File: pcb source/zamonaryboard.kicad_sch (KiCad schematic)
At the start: 25 parts, among them J1 USB_C_Receptacle_USB2.0_14P, SW1 SW_Push, U1 ESP32-S2, U2 ME6211C33M5, Y1 Crystal_GND24

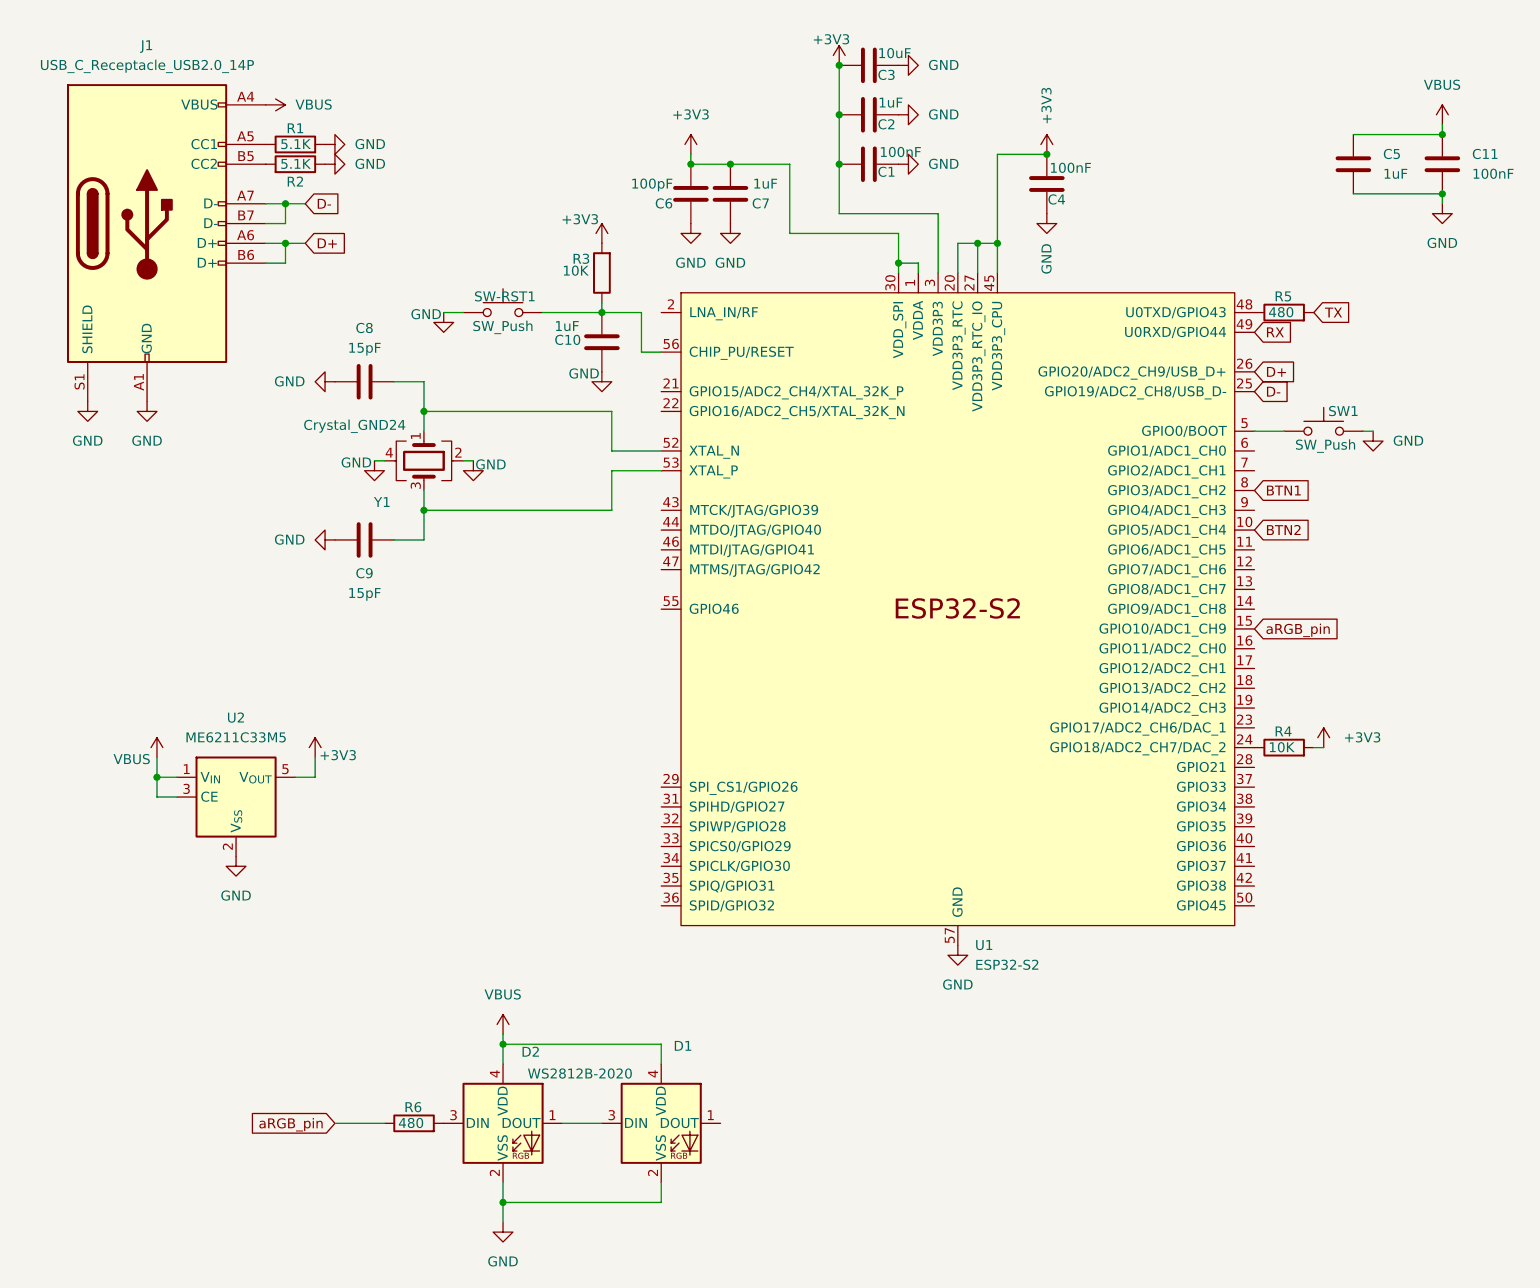
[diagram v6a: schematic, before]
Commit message: Testing of auto-release of firmware
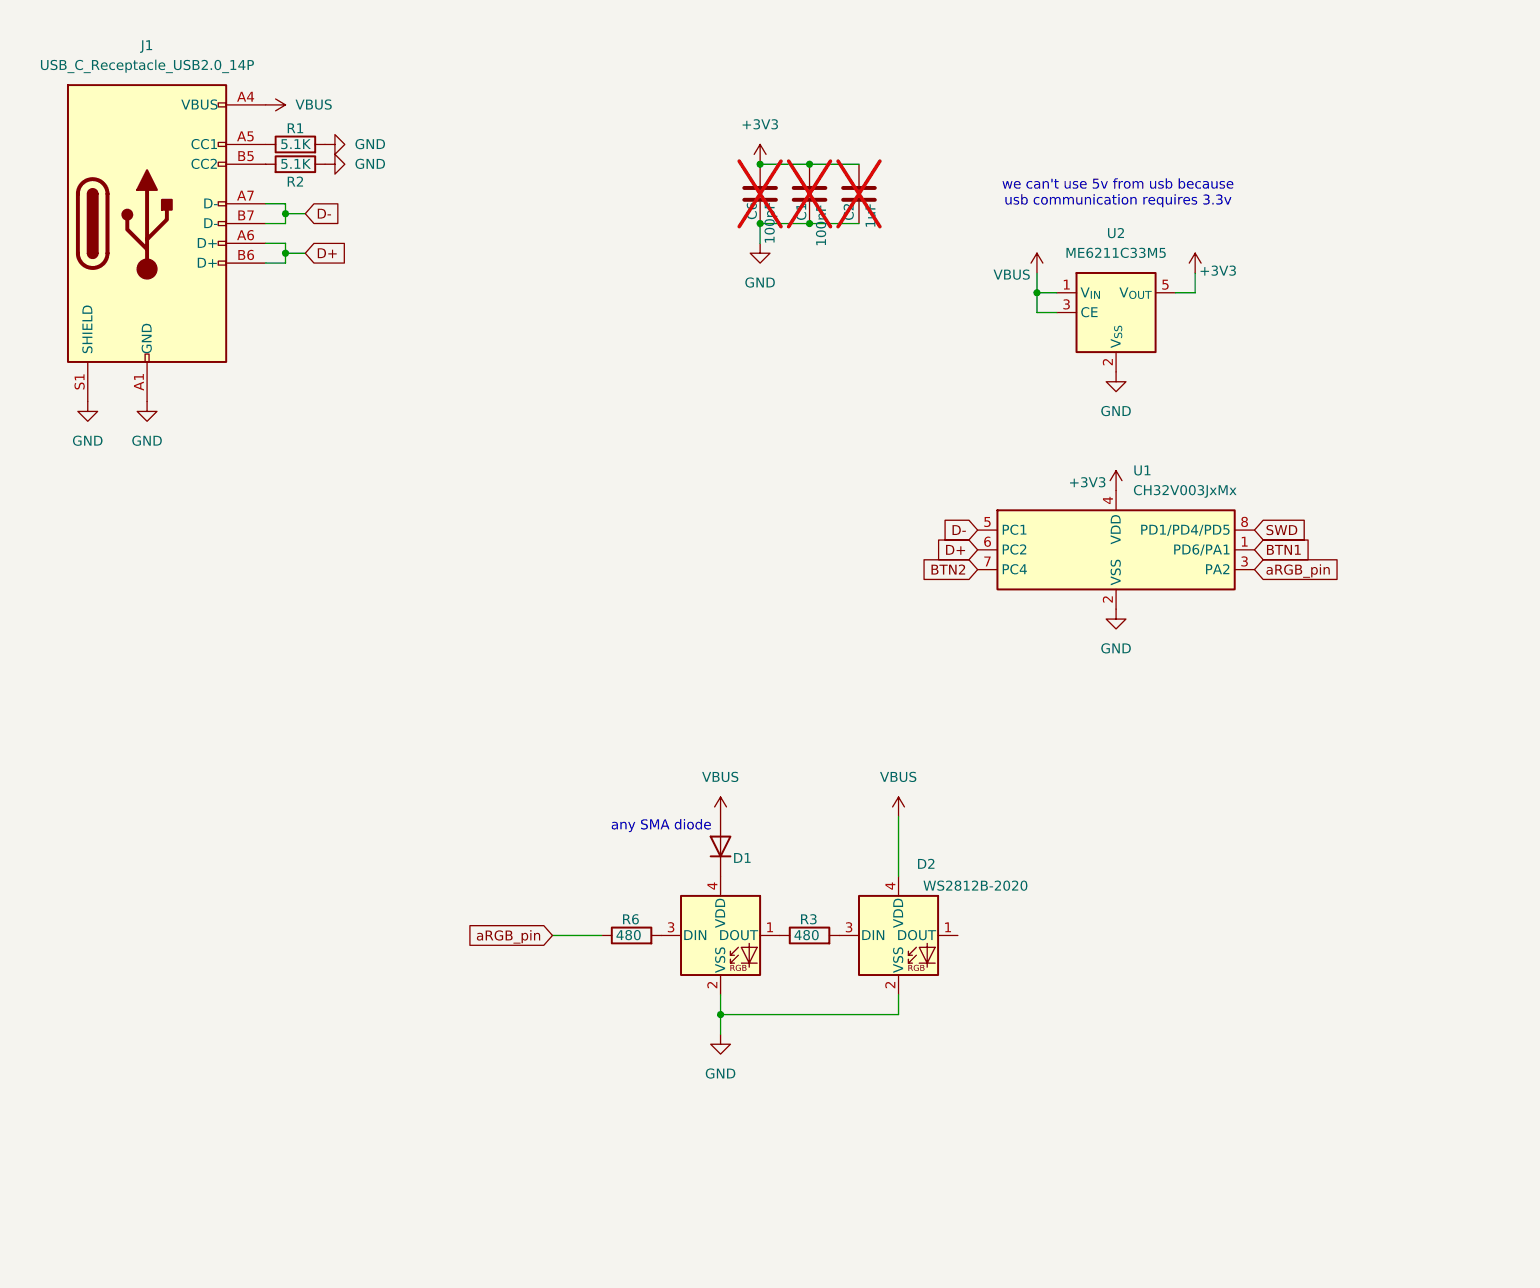
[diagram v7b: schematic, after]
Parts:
- removed C10, C5, C7: 1uF, Capacitor_SMD:C_0603_1608Metric, symbol Device:C
- removed C11, C4: 100nF, Capacitor_SMD:C_0603_1608Metric, symbol Device:C
- removed C3: 10uF, Capacitor_SMD:C_0603_1608Metric, symbol Device:C
- removed C8, C9: 15pF, Capacitor_SMD:C_0603_1608Metric, symbol Device:C
- removed R4: 10K, Resistor_SMD:R_0603_1608Metric, symbol Device:R
- removed R5: 480, Resistor_SMD:R_0603_1608Metric, symbol Device:R
- removed SW-RST1, SW1: SW_Push, Button_Switch_SMD:SW_SPST_SKQG_WithoutStem, symbol Switch:SW_Push
- removed U1: ESP32-S2, Package_DFN_QFN:QFN-56-1EP_7x7mm_P0.4mm_EP5.6x5.6mm, symbol PCM_Espressif:ESP32-S2
- removed Y1: Crystal_GND24, Crystal:Crystal_SMD_3225-4Pin_3.2x2.5mm, symbol Device:Crystal_GND24
- added D3: US1B, Diode_SMD:D_SMA, symbol Diode:US1B
- added U1: CH32V003JxMx, Package_SO:SOP-8_3.9x4.9mm_P1.27mm, symbol MCU_WCH_CH32V0:CH32V003JxMx
- C1, C2, C6: now not fitted
- J1: footprint Connector_USB:USB_C_Receptacle_GCT_USB4105-xx-A_16P_TopMnt_Horizontal -> Connector_USB:USB_C_Receptacle_GCT_USB4110
- R3: value 10K -> 480
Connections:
- net +3V3: now also U1.4 (VDD); no longer R3.2
- net BTN1: now also U1.1 (PD6/PA1)
- net BTN2: now also U1.7 (PC4)
- net D+: now also U1.6 (PC2)
- net D-: now also U1.5 (PC1)
- net GND: now also U1.2 (VSS)
- net VBUS: now also D3.2 (A); no longer D1.4 (VDD)
- net aRGB_pin: now also U1.3 (PA2)
- net at R3.1: now also D1.1 (DOUT)
- net at D2.1 (DOUT): no longer D1.3 (DIN)
- net at D2.3 (DIN): now also R3.2; no longer R6.2
- new net: D1.4 (VDD), D3.1 (K)
- new net: D1.3 (DIN), R6.2
- new net SWD: U1.8 (PD1/PD4/PD5)
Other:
- note added: "any SMA diode"
- note added: "we can't use 5v from usb because usb communication requires 3.3v"
- moved on the sheet: D1, D2, R6, U2
